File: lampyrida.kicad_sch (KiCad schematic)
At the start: 15 parts, among them K1 SW_Push_45deg, K2 SW_Push_45deg, K3 SW_Push_45deg, K4 SW_Push_45deg, U1 RP2040 Zero, U2 TXB0101DBV

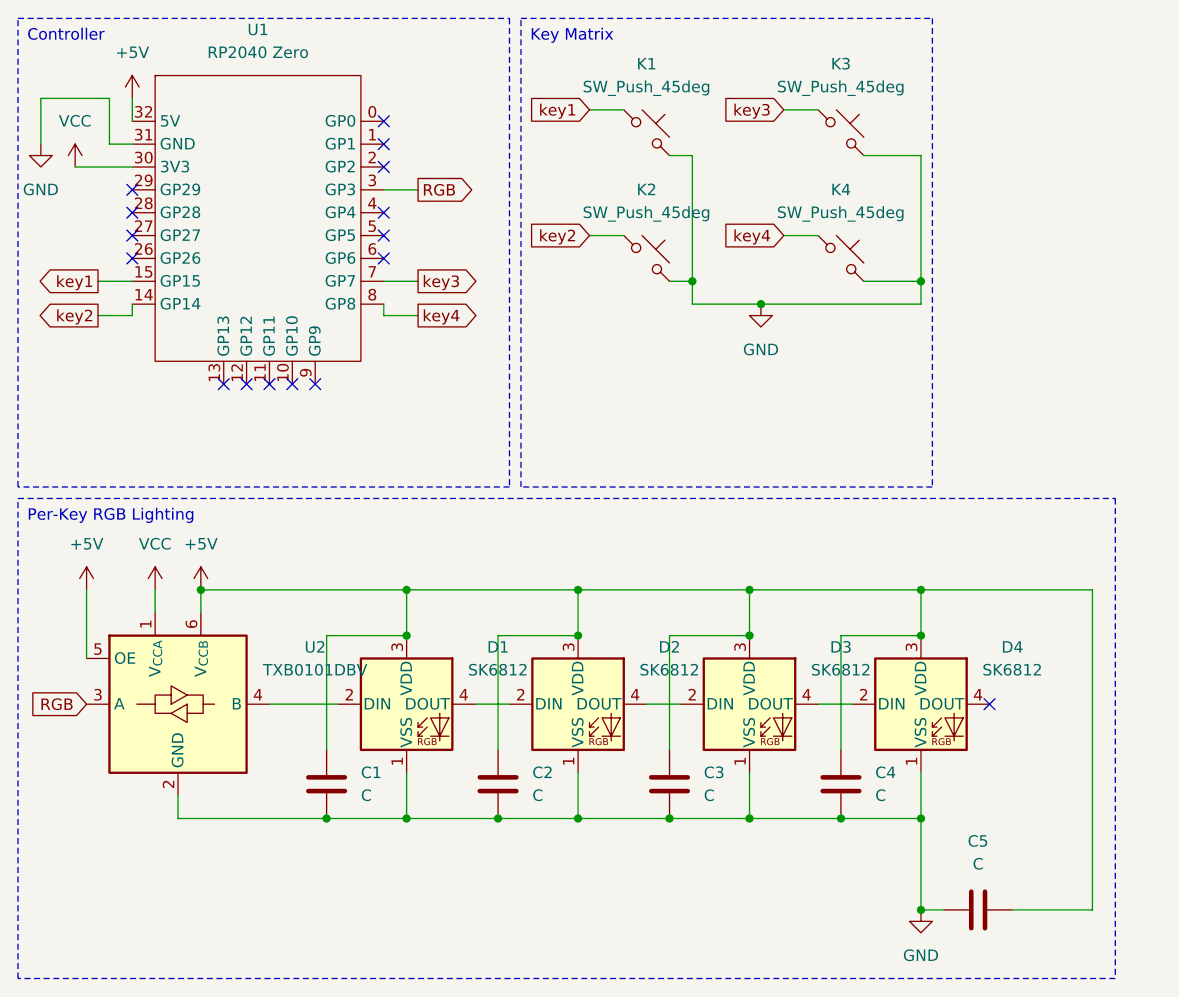
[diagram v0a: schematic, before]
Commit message: Add R1, improve ground plane, add labels.
Fixes #7 by making more room for the ground pour to go around things
and with some better-placed vias.

Fixes #6 by adding labels, both in schematic and PCB, for capacitors
and the new resistor.

Fixes #5 by adding a spot for a 500-ish Ohm resistor on the LED data
input line.

Fixes #2 by moving C1 further away from the LED footprint.
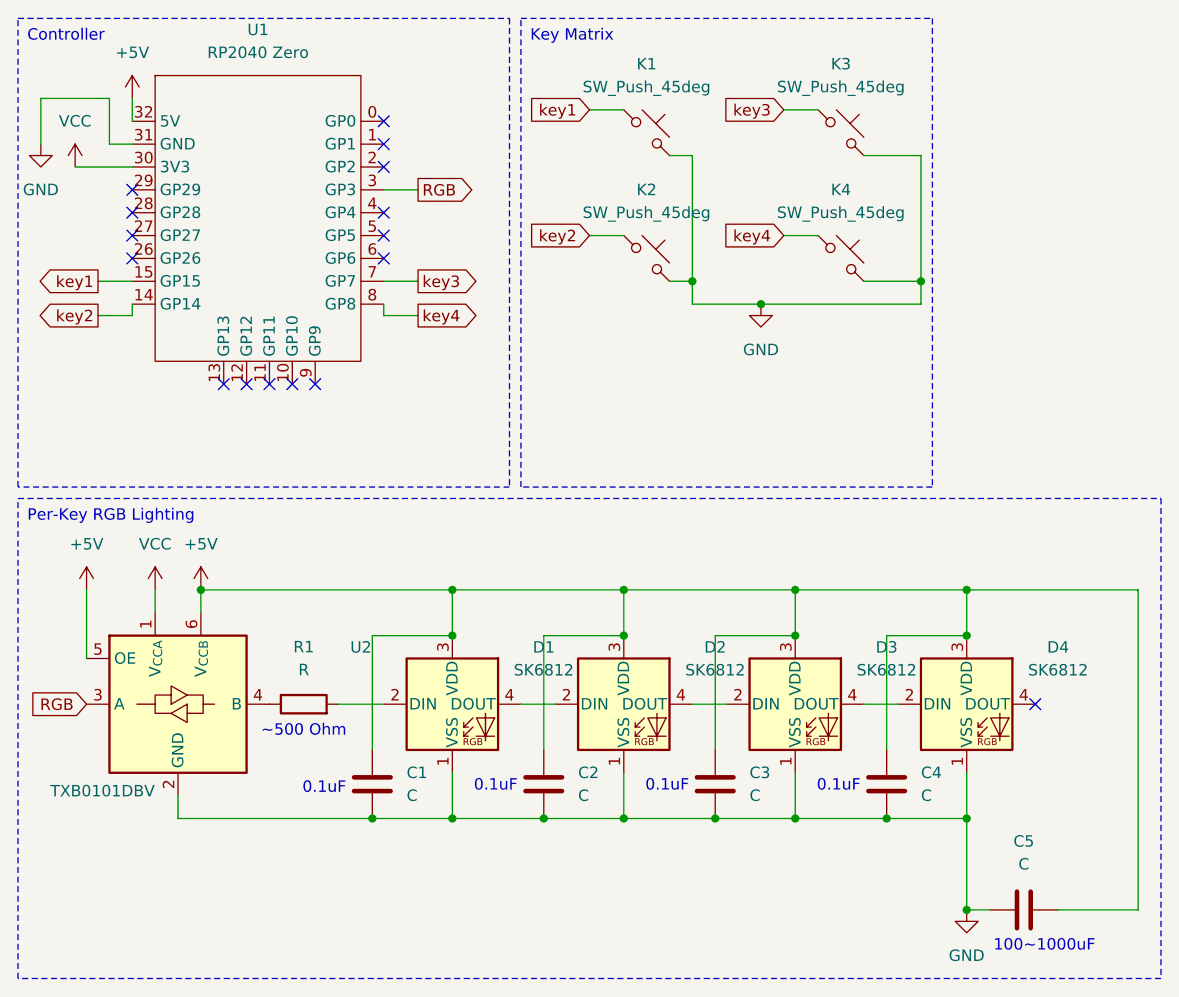
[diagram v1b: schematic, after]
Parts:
- added R1: R, Resistor_SMD:R_1206_3216Metric_Pad1.30x1.75mm_HandSolder, symbol Device:R
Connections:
- net at U2.4 (B): now also R1.1; no longer D1.2 (DIN)
- new net: D1.2 (DIN), R1.2
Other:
- note added: "0.1uF"
- note added: "100~1000uF"
- note added: "~500 Ohm"
- moved on the sheet: C1, C2, C3, C4, C5, D1, D2, D3, D4

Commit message: Fixes #4 by swapping which end of K3 and K4 is connected to ground.
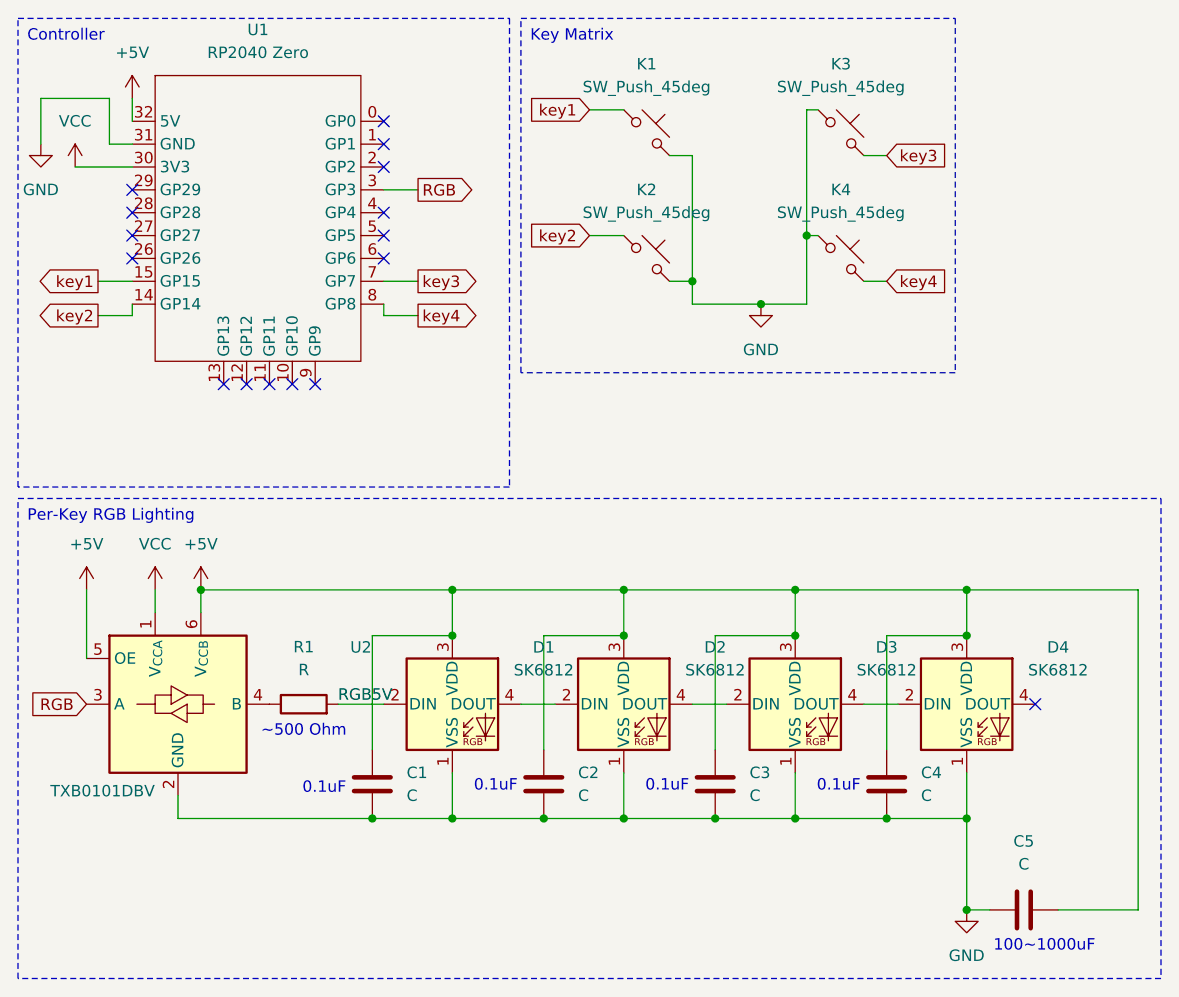
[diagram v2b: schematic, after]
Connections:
- net GND: now also K3.1, K4.1; no longer K3.2, K4.2
- net key3: now also K3.2; no longer K3.1
- net key4: now also K4.2; no longer K4.1
- net RGB5V: now reaches D1.2 (DIN), R1.2
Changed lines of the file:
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@@
-	)
-	(junction
-		(at 116.84 44.45)
-		(diameter 0)
-		(color 0 0 0 0)
 	)
 	(junction
@@
 	)
 	(junction
+		(at 104.14 39.37)
+		(diameter 0)
+		(color 0 0 0 0)
+	)
+	(junction
 		(at 93.98 104.14)
 		(diameter 0)
@@
 	(wire
 		(pts
+			(xy 104.14 39.37) (xy 105.41 39.37)
+		)
+		(stroke
+			(width 0)
+			(type default)
+		)
+	)
+	(wire
+		(pts
 			(xy 91.44 46.99) (xy 99.06 46.99)
 		)
@@
 	(wire
 		(pts
-			(xy 99.06 46.99) (xy 116.84 46.99)
-		)
-		(stroke
-			(width 0)
-			(type default)
-		)
-	)
-	(wire
-		(pts
-			(xy 101.6 25.4) (xy 105.41 25.4)
-		)
-		(stroke
-			(width 0)
-			(type default)
-		)
-	)
-	(wire
-		(pts
-			(xy 116.84 30.48) (xy 110.49 30.48)
+			(xy 99.06 46.99) (xy 104.14 46.99)
 		)
 		(stroke
@@
 	(wire
 		(pts
+			(xy 104.14 25.4) (xy 104.14 39.37)
+		)
+		(stroke
+			(width 0)
+			(type default)
+		)
+	)
+	(wire
+		(pts
 			(xy 88.9 30.48) (xy 91.44 30.48)
 		)
@@
 	(wire
 		(pts
+			(xy 110.49 30.48) (xy 113.03 30.48)
+		)
+		(stroke
+			(width 0)
+			(type default)
+		)
+	)
+	(wire
+		(pts
 			(xy 140.97 114.3) (xy 140.97 78.74)
 		)
@@
 	(wire
 		(pts
-			(xy 116.84 46.99) (xy 116.84 44.45)
-		)
-		(stroke
-			(width 0)
-			(type default)
-		)
-	)
-	(wire
-		(pts
 			(xy 64.77 99.06) (xy 64.77 104.14)
 		)
@@
 	(wire
 		(pts
+			(xy 104.14 39.37) (xy 104.14 46.99)
+		)
+		(stroke
+			(width 0)
+			(type default)
+		)
+	)
+	(wire
+		(pts
 			(xy 91.44 46.99) (xy 91.44 44.45)
 		)
@@
 	(wire
 		(pts
-			(xy 116.84 44.45) (xy 116.84 30.48)
-		)
-		(stroke
-			(width 0)
-			(type default)
-		)
-	)
-	(wire
-		(pts
 			(xy 110.49 91.44) (xy 114.3 91.44)
 		)
@@
 	(wire
 		(pts
-			(xy 110.49 44.45) (xy 116.84 44.45)
-		)
-		(stroke
-			(width 0)
-			(type default)
-		)
-	)
-	(wire
-		(pts
 			(xy 140.97 114.3) (xy 132.08 114.3)
 		)
@@
 	(wire
 		(pts
+			(xy 105.41 25.4) (xy 104.14 25.4)
+		)
+		(stroke
+			(width 0)
+			(type default)
+		)
+	)
+	(wire
+		(pts
 			(xy 19.05 24.13) (xy 19.05 29.21)
 		)
@@
 	(wire
 		(pts
+			(xy 110.49 44.45) (xy 113.03 44.45)
+		)
+		(stroke
+			(width 0)
+			(type default)
+		)
+	)
+	(wire
+		(pts
 			(xy 121.92 104.14) (xy 121.92 114.3)
 		)
@@
 		(pts
 			(xy 74.93 96.52) (xy 74.93 83.82)
-		)
-		(stroke
-			(width 0)
-			(type default)
-		)
-	)
-	(wire
-		(pts
-			(xy 101.6 39.37) (xy 105.41 39.37)
 		)
 		(stroke
@@
 		(exclude_from_sim no)
 		(at 72.39 15.24 0)
-		(size 45.72 52.07)
+		(size 48.26 39.37)
 		(stroke
 			(width 0)
@@
 				(size 1.27 1.27)
 			)
+		)
+	)
+	(label "RGB5V"
+		(at 52.07 91.44 0)
+		(fields_autoplaced yes)
+		(effects
+			(font
+				(size 1.27 1.27)
+			)
+			(justify left bottom)
 		)
 	)
@@
 	(global_label "key4"
 		(shape input)
-		(at 101.6 39.37 180)
+		(at 113.03 44.45 0)
 		(fields_autoplaced yes)
 		(effects
@@
 				(size 1.27 1.27)
 			)
-			(justify right)
+			(justify left)
 		)
 		(property "Intersheetrefs" "${INTERSHEET_REFS}"
-			(at 94.321 39.37 0)
+			(at 120.309 44.45 0)
 			(effects
 				(font
 					(size 1.27 1.27)
 				)
-				(justify right)
+				(justify left)
 				(hide yes)
 			)
@@
 	(global_label "key3"
 		(shape input)
-		(at 101.6 25.4 180)
+		(at 113.03 30.48 0)
 		(fields_autoplaced yes)
 		(effects
@@
 				(size 1.27 1.27)
 			)
-			(justify right)
+			(justify left)
 		)
 		(property "Intersheetrefs" "${INTERSHEET_REFS}"
-			(at 94.321 25.4 0)
+			(at 120.309 30.48 0)
 			(effects
 				(font
 					(size 1.27 1.27)
 				)
-				(justify right)
+				(justify left)
 				(hide yes)
 			)

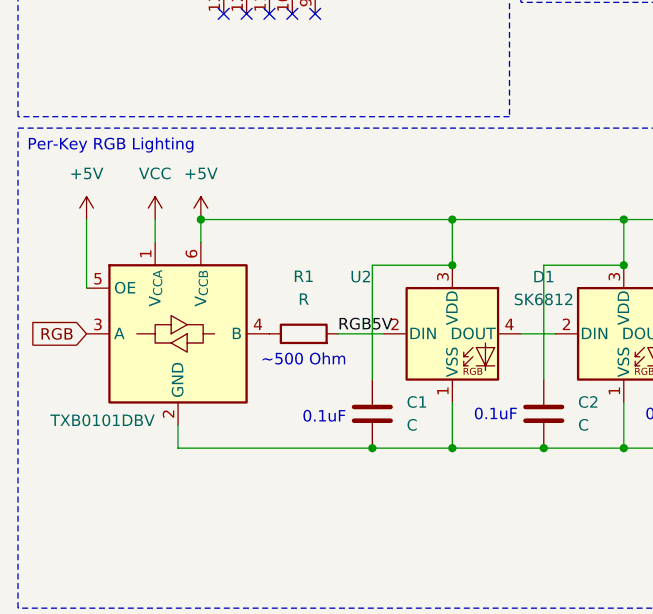
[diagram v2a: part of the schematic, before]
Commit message: Removing level shifter to use 3.3V power and signal with SK2812 LEDs.
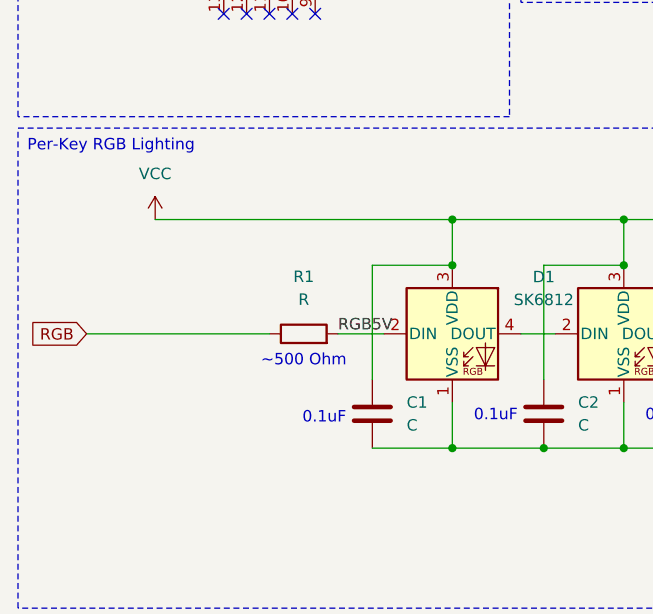
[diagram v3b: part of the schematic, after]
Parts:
- removed U2: TXB0101DBV, Package_TO_SOT_SMD:SOT-23-6, symbol Logic_LevelTranslator:TXB0101DBV
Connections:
- net +5V: no longer C1.2, C2.2, C3.2, C4.2, C5.1, D1.3 (VDD), D2.3 (VDD), D3.3 (VDD), D4.3 (VDD)
- net RGB: now also R1.1
- net VCC: now also C1.2, C2.2, C3.2, C4.2, C5.1, D1.3 (VDD), D2.3 (VDD), D3.3 (VDD), D4.3 (VDD)

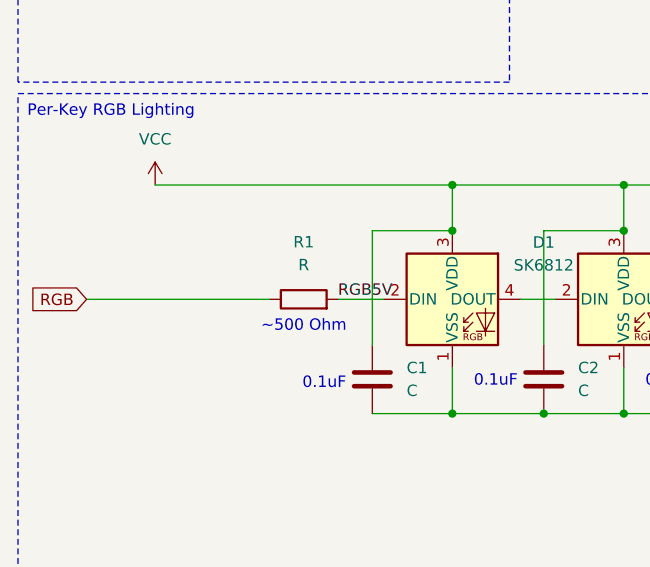
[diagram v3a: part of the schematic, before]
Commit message: Rerouting traces with new non-5V net.
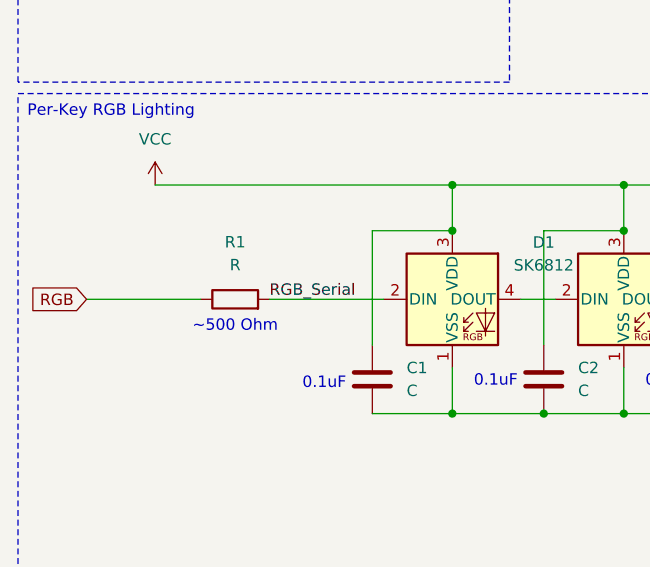
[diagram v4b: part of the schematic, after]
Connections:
- net RGB5V renamed RGB_Serial
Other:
- moved on the sheet: R1
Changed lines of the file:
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@@
 	(wire
 		(pts
-			(xy 24.13 91.44) (xy 44.45 91.44)
+			(xy 24.13 91.44) (xy 36.83 91.44)
 		)
 		(stroke
@@
 	(wire
 		(pts
-			(xy 52.07 91.44) (xy 57.15 91.44)
+			(xy 44.45 91.44) (xy 57.15 91.44)
 		)
 		(stroke
@@
 	(text "~500 Ohm"
 		(exclude_from_sim no)
-		(at 48.26 94.488 0)
+		(at 40.64 94.488 0)
 		(effects
 			(font
@@
 		)
 	)
-	(label "RGB5V"
-		(at 52.07 91.44 0)
+	(label "RGB_Serial"
+		(at 44.45 91.44 0)
 		(fields_autoplaced yes)
 		(effects
@@
 	(symbol
 		(lib_id "Device:R")
-		(at 48.26 91.44 90)
+		(at 40.64 91.44 90)
 		(unit 1)
 		(exclude_from_sim no)
@@
 		(fields_autoplaced yes)
 		(property "Reference" "R1"
-			(at 48.26 85.09 90)
+			(at 40.64 85.09 90)
 			(effects
 				(font
@@
 		)
 		(property "Value" "R"
-			(at 48.26 87.63 90)
+			(at 40.64 87.63 90)
 			(effects
 				(font
@@
 		)
 		(property "Footprint" "Resistor_SMD:R_1206_3216Metric_Pad1.30x1.75mm_HandSolder"
-			(at 48.26 93.218 90)
+			(at 40.64 93.218 90)
 			(effects
 				(font
@@
 		)
 		(property "Datasheet" "~"
-			(at 48.26 91.44 0)
+			(at 40.64 91.44 0)
 			(effects
 				(font
@@
 		)
 		(property "Description" "Resistor"
-			(at 48.26 91.44 0)
-			(effects
-				(font
+			(at 40.64 91.44 0)
+			(effects
+				(font
